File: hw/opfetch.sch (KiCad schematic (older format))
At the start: 5 parts, among them U401 74HC00, U402 74HC193, U403 74HC02, U404 74HC175, U405 74HC574

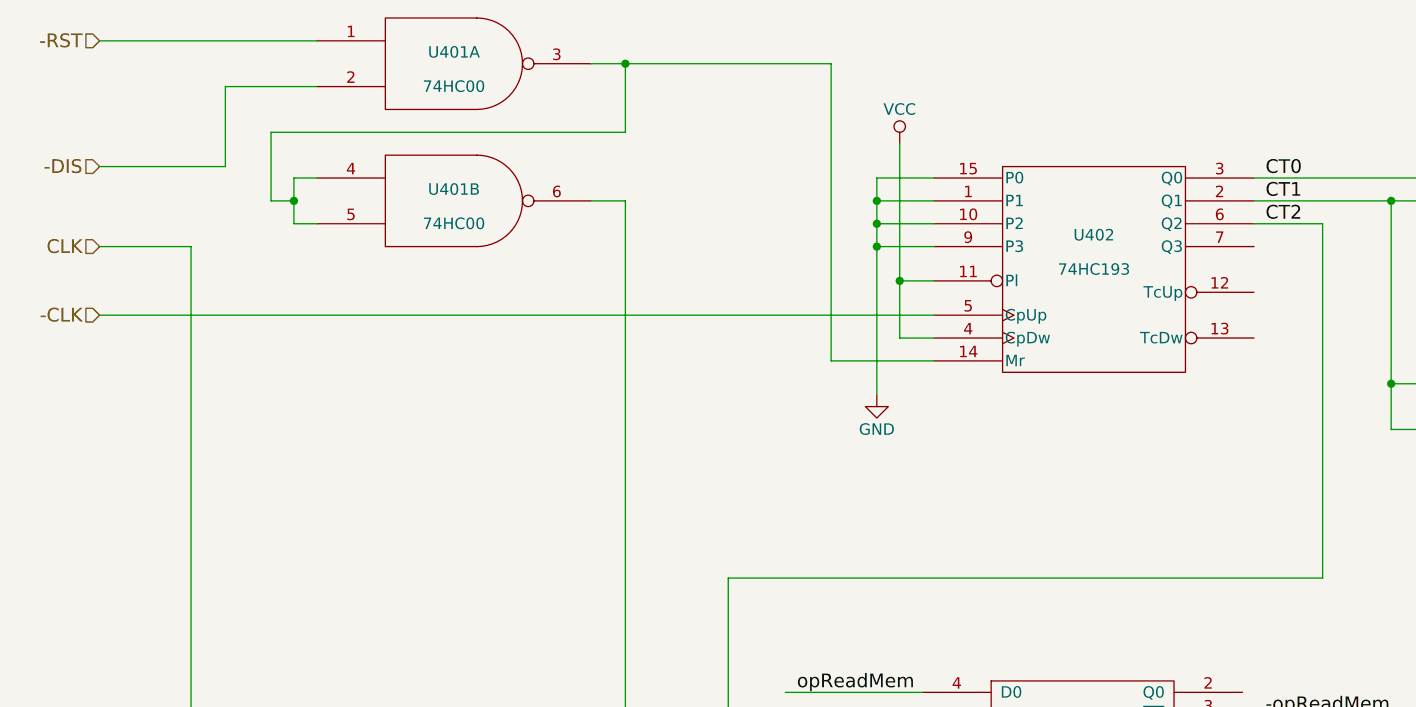
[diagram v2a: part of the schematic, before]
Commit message: replace '193 with '393 in opfetch module
The '393 has two fewer pins, better use of breadboard space.
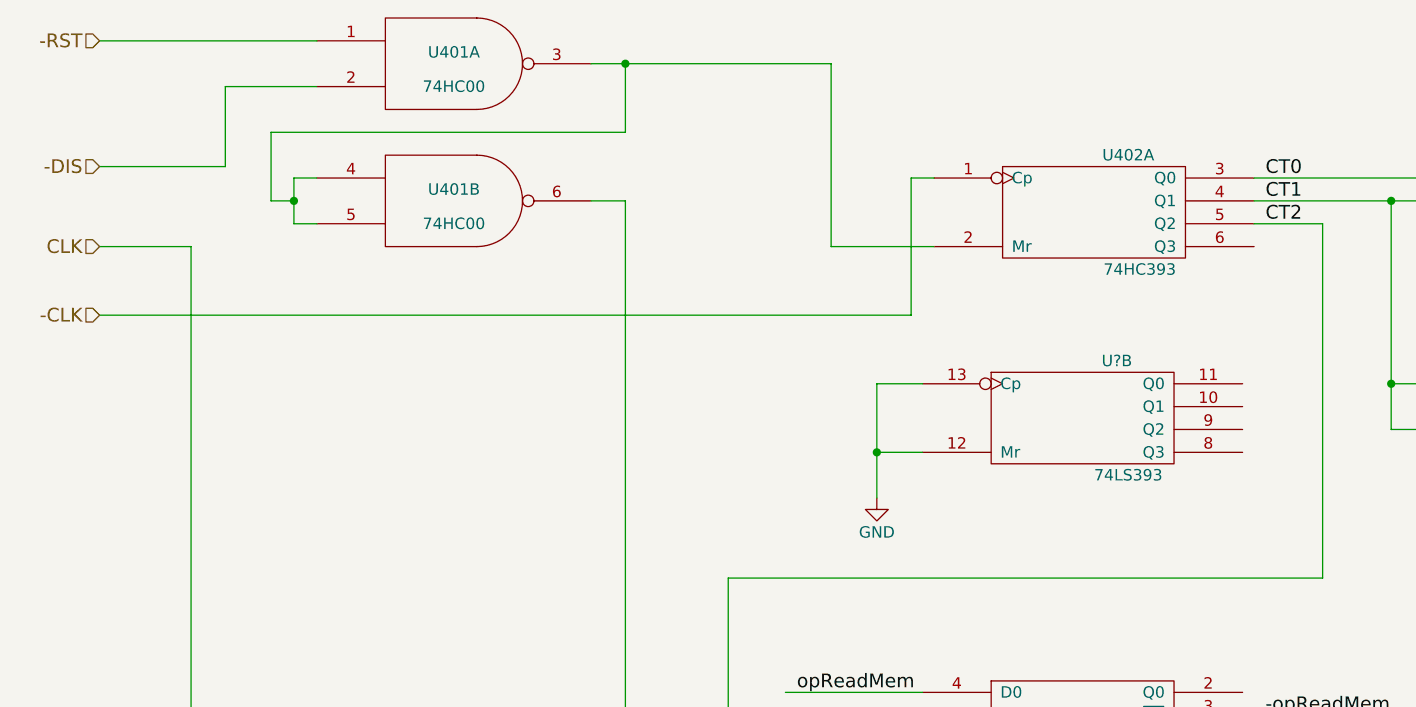
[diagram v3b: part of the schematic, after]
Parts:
- removed U402: 74HC193, symbol 74LS193
- added U402: 74HC393, symbol 74LS393
- added U?: 74LS393, symbol 74LS393
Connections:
- net labels removed: VCC
- wire segments 91 -> 88
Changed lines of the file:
@@
-$EndComp
-$Comp
-L 74LS193 U402
-U 1 1 59284D07
-P 5450 1900
-F 0 "U402" H 5450 2050 50  0000 C CNN
-F 1 "74HC193" H 5450 1900 50  0000 C CNN
-F 2 "" H 5450 1900 50  0001 C CNN
-F 3 "" H 5450 1900 50  0001 C CNN
-	1    5450 1900
-	1    0    0    -1
 $EndComp
 $Comp
@@
 ALU7
 $Comp
-L VCC #PWR?
-U 1 1 59285A53
-P 4600 1350
-F 0 "#PWR?" H 4600 1200 50  0001 C CNN
-F 1 "VCC" H 4600 1500 50  0000 C CNN
-F 2 "" H 4600 1350 50  0001 C CNN
-F 3 "" H 4600 1350 50  0001 C CNN
-	1    4600 1350
-	1    0    0    -1
-$EndComp
-$Comp
-L GND #PWR?
-U 1 1 59285A95
-P 4500 2450
-F 0 "#PWR?" H 4500 2200 50  0001 C CNN
-F 1 "GND" H 4500 2300 50  0000 C CNN
-F 2 "" H 4500 2450 50  0001 C CNN
-F 3 "" H 4500 2450 50  0001 C CNN
-	1    4500 2450
-	1    0    0    -1
-$EndComp
-$Comp
 L 74LS02 U403
 U 1 1 59285C63
@@
 Connection ~ 1950 1600
 Wire Wire Line
-	4750 2300 4300 2300
-Wire Wire Line
-	4300 2300 4300 1000
+	4750 1800 4300 1800
+Wire Wire Line
+	4300 1800 4300 1000
 Wire Wire Line
 	3400 1600 3400 4650
@@
 	3400 4650 4700 4650
 Wire Wire Line
-	1100 2100 4750 2100
+	1100 2100 4650 2100
 Wire Wire Line
 	1500 4550 4700 4550
@@
 Wire Wire Line
 	1500 1800 1100 1800
-Wire Wire Line
-	4600 2200 4750 2200
-Wire Wire Line
-	4600 1350 4600 2200
-Wire Wire Line
-	4750 1950 4600 1950
-Connection ~ 4600 1950
-Wire Wire Line
-	4500 1800 4750 1800
-Wire Wire Line
-	4500 1500 4500 2450
-Wire Wire Line
-	4750 1700 4500 1700
-Connection ~ 4500 1800
-Wire Wire Line
-	4750 1600 4500 1600
-Connection ~ 4500 1700
-Wire Wire Line
-	4750 1500 4500 1500
-Connection ~ 4500 1600
 Wire Wire Line
 	6150 1500 7500 1500
@@
 Text HLabel 10000 4450 2    60   Output ~ 0
 opIncPC
+$Comp
+L 74LS393 U402
+U 1 1 598D274D
+P 5450 1650
+F 0 "U402" H 5600 1900 50  0000 C CNN
+F 1 "74HC393" H 5650 1400 50  0000 C CNN
+F 2 "" H 5450 1650 50  0001 C CNN
+F 3 "" H 5450 1650 50  0001 C CNN
+	1    5450 1650
+	1    0    0    -1
+$EndComp
+Wire Wire Line
+	4650 2100 4650 1500
+Wire Wire Line
+	4650 1500 4750 1500
+$Comp
+L 74LS393 U?
+U 2 1 598D4BE5
+P 5400 2550
+F 0 "U?" H 5550 2800 50  0000 C CNN
+F 1 "74LS393" H 5600 2300 50  0000 C CNN
+F 2 "" H 5400 2550 50  0001 C CNN
+F 3 "" H 5400 2550 50  0001 C CNN
+	2    5400 2550
+	1    0    0    -1
+$EndComp
+Wire Wire Line
+	4700 2400 4500 2400
+Wire Wire Line
+	4500 2400 4500 2900
+Wire Wire Line
+	4700 2700 4500 2700
+Connection ~ 4500 2700
+$Comp
+L GND #PWR?
+U 1 1 598D4CFA
+P 4500 2900
+F 0 "#PWR?" H 4500 2650 50  0001 C CNN
+F 1 "GND" H 4500 2750 50  0000 C CNN
+F 2 "" H 4500 2900 50  0001 C CNN
+F 3 "" H 4500 2900 50  0001 C CNN
+	1    4500 2900
+	1    0    0    -1
+$EndComp
 $EndSCHEMATC
